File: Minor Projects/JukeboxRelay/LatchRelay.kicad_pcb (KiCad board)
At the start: 2 copper layers, 36.8 x 30.5 mm, 6 parts, among them J1 Relay Socket, K1 AZ850P2-x

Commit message: Completed JukeBox and SpaceInvader PCBs Created Gerbers Ordered Parts
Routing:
- net Net-(J1-Pad6): track 0.00 -> 9.73 mm
- removed copper zone on B.Cu, net Net-(J1-Pad6)
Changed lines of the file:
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@@
     (thickness 1.6)
     (drawings 6)
-    (tracks 54)
+    (tracks 60)
     (zones 0)
     (modules 6)
@@
     (visible_elements FFFFFFFF)
     (pcbplotparams
-      (layerselection 0x010fc_ffffffff)
-      (usegerberextensions false)
+      (layerselection 0x010f0_ffffffff)
+      (usegerberextensions true)
       (usegerberattributes false)
       (usegerberadvancedattributes false)
@@
       (outputformat 1)
       (mirror false)
-      (drillshape 1)
+      (drillshape 0)
       (scaleselection 1)
-      (outputdirectory ""))
+      (outputdirectory Gerber/))
   )
   (net 0 "")
@@
   (segment (start 134 90.155) (end 140.335 83.82) (width 1.25) (layer F.Cu) (net 10) (status C00000))
   (segment (start 140.335 83.82) (end 140.97 83.82) (width 1.25) (layer F.Cu) (net 10) (status C00000))
+  (segment (start 137.5 90.17) (end 137.5 90.084) (width 1.25) (layer F.Cu) (net 11) (status C00000))
+  (segment (start 137.5 90.084) (end 141.732 85.852) (width 1.25) (layer F.Cu) (net 11) (status 400000))
+  (segment (start 142.24 85.852) (end 143.51 84.582) (width 1.25) (layer F.Cu) (net 11) (status 800000))
+  (segment (start 141.732 85.852) (end 142.24 85.852) (width 1.25) (layer F.Cu) (net 11))
+  (segment (start 143.51 84.582) (end 143.51 83.82) (width 1.25) (layer F.Cu) (net 11) (status C00000))
+  (segment (start 137.5 90.17) (end 137.5 89.576) (width 1.25) (layer B.Cu) (net 11) (status C00000))
   (segment (start 146.05 83.82) (end 146.05 85.12) (width 1.25) (layer F.Cu) (net 12) (status 400000))
   (segment (start 146.05 85.12) (end 141 90.17) (width 1.25) (layer F.Cu) (net 12) (status 800000))
-  (zone (net 11) (net_name "Net-(J1-Pad6)") (layer B.Cu) (hatch edge 0.508)
-    (connect_pads (clearance 0.508))
-    (min_thickness 0.254)
-    (fill yes (arc_segments 16) (thermal_gap 0.508) (thermal_bridge_width 0.508))
-    (polygon
-      (pts
-        (xy 122.936 63.5) (xy 122.936 95.504) (xy 163.068 95.504) (xy 162.56 63.5) (xy 123.444 63.5)
-      )
-    )
-  )
 )

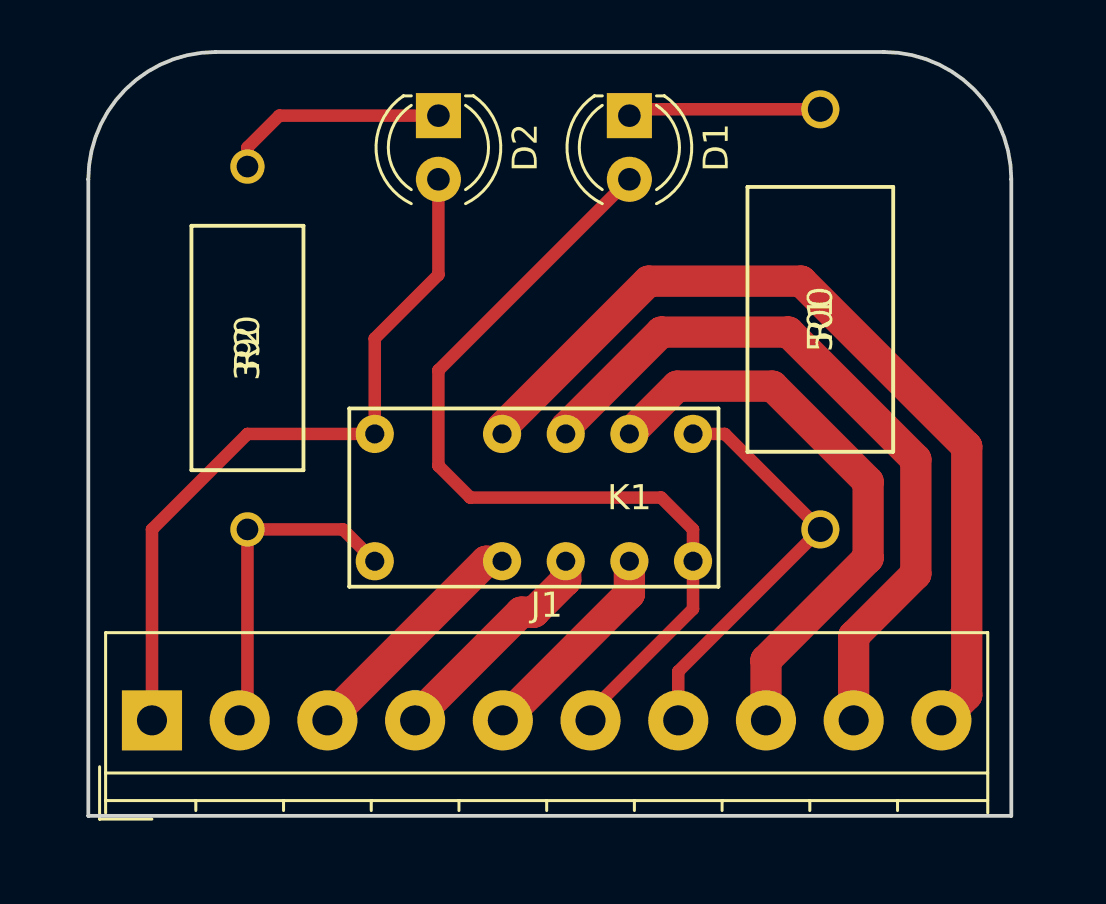
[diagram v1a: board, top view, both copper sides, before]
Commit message: Finalized PCB Designs for Relay and Space Invaders and ordered them
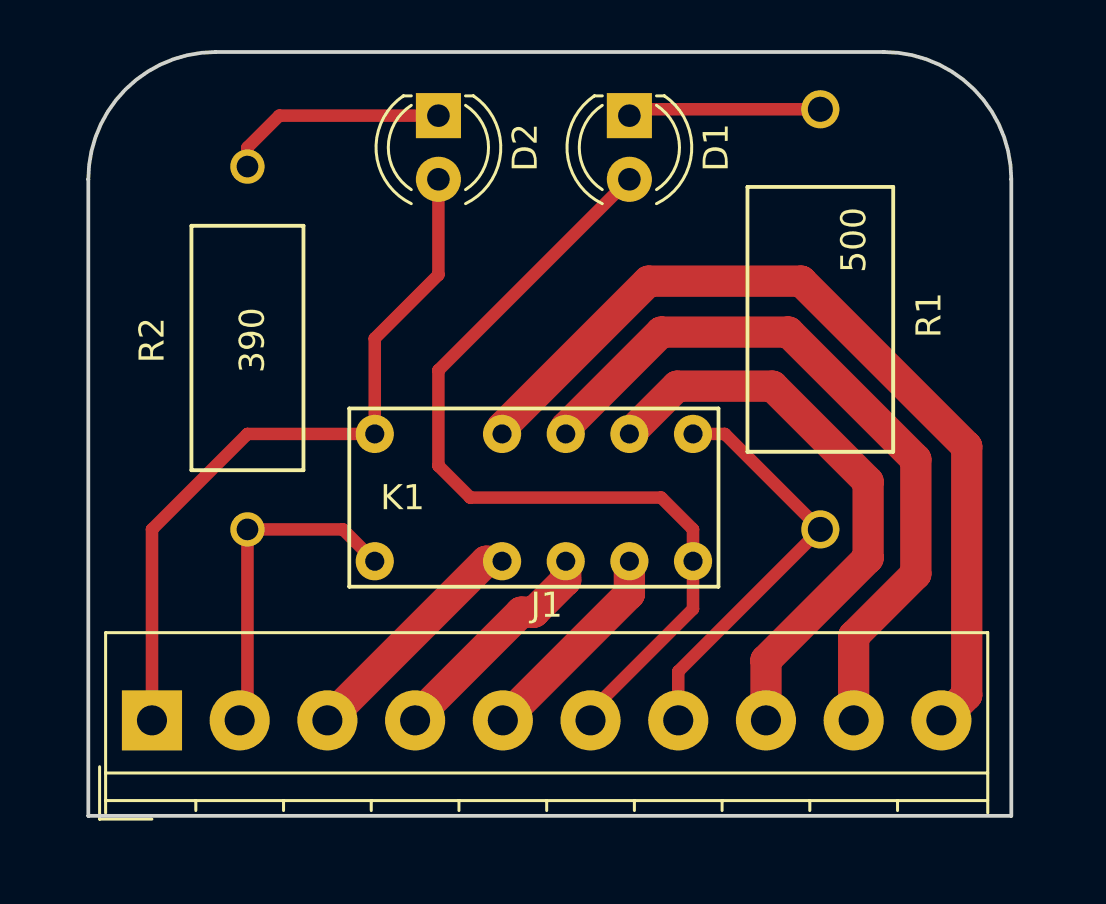
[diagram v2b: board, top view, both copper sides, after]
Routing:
- net Net-(J1-Pad6): track 9.73 -> 9.14 mm
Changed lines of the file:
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@@
-(kicad_pcb (version 20171130) (host pcbnew "(2017-12-24 revision 570866557)-makepkg")
+(kicad_pcb (version 20171130) (host pcbnew "(5.0.0-rc2-dev-720-g9704891c8)")
   (general
     (thickness 1.6)
     (drawings 6)
-    (tracks 60)
+    (tracks 59)
     (zones 0)
     (modules 6)
@@
     (visible_elements FFFFFFFF)
     (pcbplotparams
-      (layerselection 0x010f0_ffffffff)
+      (layerselection 0x010e0_7fffffff)
       (usegerberextensions true)
-      (usegerberattributes false)
+      (usegerberattributes true)
       (usegerberadvancedattributes false)
       (creategerberjobfile false)
@@
   (module Library:42J500E (layer F.Cu)
     (at 153.67 82.55 270)
-    (fp_text reference R1 (at -8.382 0 270) (layer F.SilkS)
-      (effects (font (size 1 1) (thickness 0.15)))
-    )
-    (fp_text value 500 (at -8.382 0 270) (layer F.SilkS)
+    (fp_text reference R1 (at -8.55 -4.33 270) (layer F.SilkS)
+      (effects (font (size 1 1) (thickness 0.15)))
+    )
+    (fp_text value 500 (at -11.55 -1.33 270) (layer F.SilkS)
       (effects (font (size 1 1) (thickness 0.15)))
     )
@@
   (module Library:FMP200JR-52-390R (layer F.Cu)
     (at 130.81 82.55 270)
-    (fp_text reference R2 (at -7.239 0 270) (layer F.SilkS)
-      (effects (font (size 1 1) (thickness 0.15)))
-    )
-    (fp_text value 390 (at -7.239 0 270) (layer F.SilkS)
+    (fp_text reference R2 (at -7.55 3.81 270) (layer F.SilkS)
+      (effects (font (size 1 1) (thickness 0.15)))
+    )
+    (fp_text value 390 (at -7.55 -0.19 270) (layer F.SilkS)
       (effects (font (size 1 1) (thickness 0.15)))
     )
@@
   (module Library:Relay (layer F.Cu)
     (at 135.89 83.82)
-    (fp_text reference K1 (at 10.16 -2.54) (layer F.SilkS)
+    (fp_text reference K1 (at 1.11 -2.54) (layer F.SilkS)
       (effects (font (size 1 1) (thickness 0.15)))
     )
@@
   (segment (start 141.732 85.852) (end 142.24 85.852) (width 1.25) (layer F.Cu) (net 11))
   (segment (start 143.51 84.582) (end 143.51 83.82) (width 1.25) (layer F.Cu) (net 11) (status C00000))
-  (segment (start 137.5 90.17) (end 137.5 89.576) (width 1.25) (layer B.Cu) (net 11) (status C00000))
   (segment (start 146.05 83.82) (end 146.05 85.12) (width 1.25) (layer F.Cu) (net 12) (status 400000))
   (segment (start 146.05 85.12) (end 141 90.17) (width 1.25) (layer F.Cu) (net 12) (status 800000))
